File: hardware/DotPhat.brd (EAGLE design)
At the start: 30 x 65 mm, 22 parts, among them CN1 1X4-BIG, J2 RASPBERRYPI-40-PIN-GPIO_PTH, J3 USB-MICROB, U1 ATMEGA328P-MU-QFN32, X3 S4B-ZR

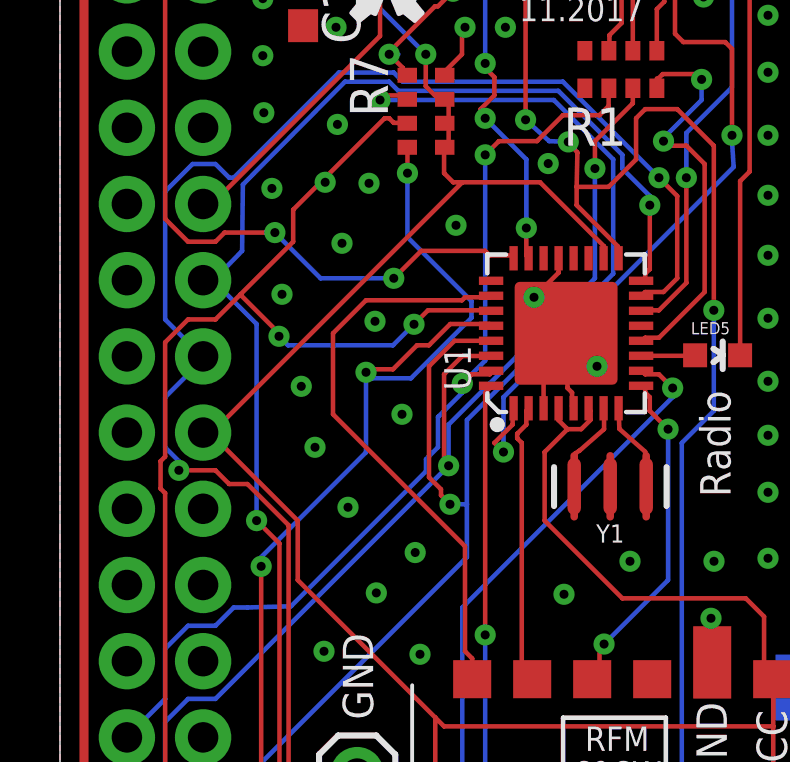
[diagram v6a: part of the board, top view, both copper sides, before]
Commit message: Add TMP112 temperature sensor
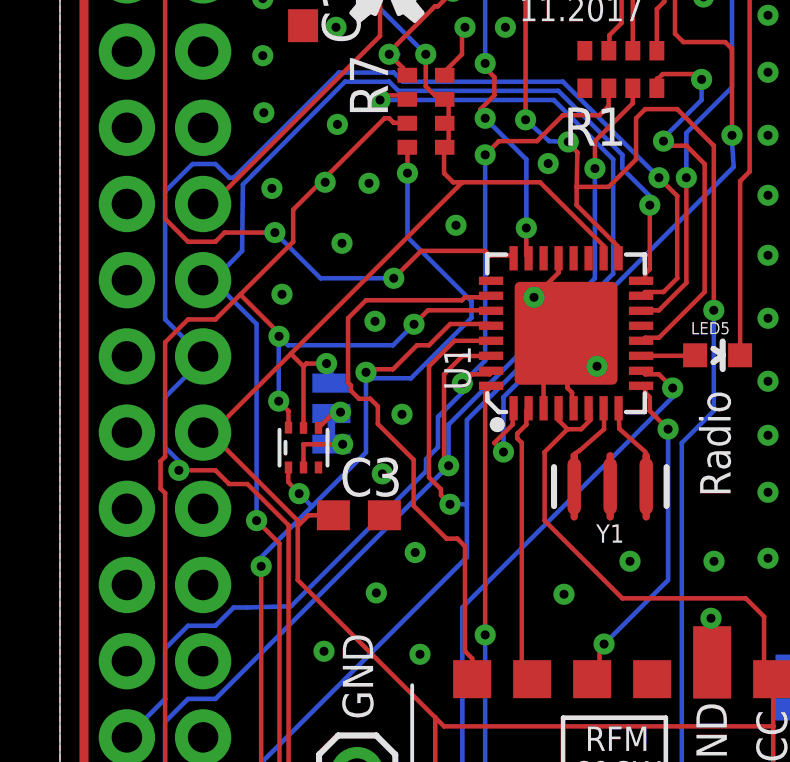
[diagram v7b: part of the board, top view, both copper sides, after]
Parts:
- added C3: 0.1uF, resistor:C0603
- added JP2: JUMPER-SMT_3_1-NC_TRACE_NO-SILK, SparkFun-Jumpers:SMT-JUMPER_3_1-NC_TRACE_NO-SILK
- added U2: TMP102, SparkFun:SOT563
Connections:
- new net N$11: JP2.2, U2.4
- net +3V3: now also C3.1, JP2.1, U2.5
- net GND: now also C3.2, JP2.3, U2.2
- net SCL: now also U2.1
- net SDA: now also U2.6
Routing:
- net +3V3: track 164.0 -> 169.5 mm, vias 3 -> 4
- net SDA: track 48.7 -> 51.9 mm, vias 3 -> 4
- net GND: track 35.2 -> 37.7 mm, vias 119 -> 118
- net SCL: track 41.2 -> 42.8 mm, vias 3 -> 4
- net N$11: track 0.00 -> 1.29 mm, vias 0 -> 1
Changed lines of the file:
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@@
 <setting verticaltext="up"/>
 </settings>
-<grid distance="0.11" unitdist="mil" unit="mil" style="lines" multiple="1" display="yes" altdistance="0.025" altunitdist="inch" altunit="inch"/>
+<grid distance="0.11" unitdist="mil" unit="mm" style="lines" multiple="1" display="yes" altdistance="0.025" altunitdist="inch" altunit="inch"/>
 <layers>
 <layer number="1" name="Top" color="4" fill="1" visible="yes" active="yes"/>
@@
 <element name="C1" library="rcl" package="C0603" value="" x="8.1026" y="43.1038" rot="R270"/>
 <element name="R1" library="SparkFun" package="0603-ARV" value="" x="18.6944" y="40.7924"/>
+<element name="U2" library="SparkFun" package="SOT563" value="TMP102" x="8.11656875" y="28.185871875"/>
+<element name="C3" library="resistor" package="C0603" value="0.1uF" x="9.963403125" y="25.9339125"/>
+<element name="JP2" library="SparkFun-Jumpers" package="SMT-JUMPER_3_1-NC_TRACE_NO-SILK" value="JUMPER-SMT_3_1-NC_TRACE_NO-SILK" x="9.044178125" y="29.32303125" rot="MR270"/>
 </elements>
 <signals>
@@
 <via x="21.8" y="24.4" extent="1-16" drill="0.3"/>
 <via x="21.7" y="22.5" extent="1-16" drill="0.3"/>
-<via x="9.6" y="26.2" extent="1-16" drill="0.3"/>
-<via x="8.5" y="28.2" extent="1-16" drill="0.3"/>
+<via x="10.745540625" y="27.31480625" extent="1-16" drill="0.3"/>
 <via x="19.3" y="15.8" extent="1-16" drill="0.3"/>
 <via x="28.9" y="19.3" extent="1-16" drill="0.3"/>
@@
 <contactref element="X3" pad="1"/>
 <contactref element="U$4" pad="2"/>
-<via x="8.0428" y="30.232" extent="1-16" drill="0.3"/>
 <via x="7.0632" y="36.8288" extent="1-16" drill="0.3"/>
 <via x="9.2476" y="38.9624" extent="1-16" drill="0.3"/>
@@
 <contactref element="C1" pad="2"/>
 <via x="14.8462" y="42.2" extent="1-16" drill="0.3"/>
+<contactref element="U2" pad="2"/>
+<contactref element="C3" pad="2"/>
+<contactref element="JP2" pad="3"/>
+<wire x1="9.044178125" y1="28.30703125" x2="9.42136875" y2="28.30703125" width="0.1524" layer="16"/>
+<wire x1="9.42136875" y1="28.30703125" x2="9.42136875" y2="28.300425" width="0.1524" layer="16"/>
+<via x="9.42136875" y="28.300425" extent="1-16" drill="0.3"/>
+<wire x1="9.42136875" y1="28.300425" x2="8.11656875" y2="28.300425" width="0.1524" layer="1"/>
+<wire x1="8.11656875" y1="28.300425" x2="8.11656875" y2="27.525871875" width="0.1524" layer="1"/>
 </signal>
 <signal name="SDA">
@@
 <wire x1="4.77" y1="10.91" x2="5.9772" y2="9.7028" width="0.1524" layer="16"/>
 <wire x1="5.9772" y1="9.7028" x2="9.906" y2="9.7028" width="0.1524" layer="16"/>
+<contactref element="U2" pad="6"/>
+<wire x1="7.61656875" y1="28.855871875" x2="7.61656875" y2="29.40951875" width="0.1524" layer="1"/>
+<wire x1="7.61656875" y1="29.40951875" x2="7.289546875" y2="29.736540625" width="0.1524" layer="1"/>
+<via x="7.289546875" y="29.736540625" extent="1-16" drill="0.3"/>
+<wire x1="7.289546875" y1="29.736540625" x2="7.289546875" y2="31.889546875" width="0.1524" layer="16"/>
+<wire x1="7.289546875" y1="31.889546875" x2="7.3" y2="31.9" width="0.1524" layer="16"/>
 </signal>
 <signal name="RST">
@@
 <wire x1="14.1256" y1="33.1756" x2="14.37" y2="33.25" width="0.1524" layer="1"/>
 <wire x1="13.716" y1="20.574" x2="13.74" y2="20.47" width="0.1524" layer="1"/>
-<wire x1="13.5" y1="24.9" x2="9.1" y2="29.3" width="0.1524" layer="1"/>
-<wire x1="9.1" y1="29.3" x2="9.1" y2="32" width="0.1524" layer="1"/>
-<wire x1="9.1" y1="32" x2="10.2" y2="33.1" width="0.1524" layer="1"/>
 <wire x1="10.2" y1="33.1" x2="13.4" y2="33.1" width="0.1524" layer="1"/>
 <wire x1="13.4" y1="33.1" x2="13.5" y2="33.2" width="0.1524" layer="1"/>
@@
 <wire x1="13.5" y1="21.4" x2="13.74" y2="21.16" width="0.1524" layer="1"/>
 <wire x1="13.74" y1="21.16" x2="13.74" y2="20.47" width="0.1524" layer="1"/>
+<wire x1="9.966196875" y1="29.81756875" x2="10.3433875" y2="29.81756875" width="0.1524" layer="1"/>
+<wire x1="10.3433875" y1="29.81756875" x2="10.594846875" y2="29.566109375" width="0.1524" layer="1"/>
+<wire x1="10.594846875" y1="29.566109375" x2="10.594846875" y2="28.976578125" width="0.1524" layer="1"/>
+<wire x1="10.594846875" y1="28.976578125" x2="11.7878875" y2="27.7835375" width="0.1524" layer="1"/>
+<wire x1="11.7878875" y1="27.7835375" x2="11.7878875" y2="26.249628125" width="0.1524" layer="1"/>
+<wire x1="11.7878875" y1="26.249628125" x2="12.883134375" y2="25.15438125" width="0.1524" layer="1"/>
+<wire x1="12.883134375" y1="25.15438125" x2="13.24561875" y2="25.15438125" width="0.1524" layer="1"/>
+<wire x1="13.24561875" y1="25.15438125" x2="13.5" y2="24.9" width="0.1524" layer="1"/>
+<wire x1="9.966196875" y1="29.81756875" x2="9.697975" y2="30.085790625" width="0.1524" layer="1"/>
+<wire x1="9.697975" y1="30.085790625" x2="9.697975" y2="30.2618125" width="0.1524" layer="1"/>
+<wire x1="9.697975" y1="30.2618125" x2="9.602978125" y2="30.356809375" width="0.1524" layer="1"/>
+<wire x1="9.602978125" y1="30.356809375" x2="9.602978125" y2="32.502978125" width="0.1524" layer="1"/>
+<wire x1="9.602978125" y1="32.502978125" x2="10.2" y2="33.1" width="0.1524" layer="1"/>
 </signal>
 <signal name="RSCK">
@@
 <wire x1="12.8016" y1="38.1" x2="12.825" y2="38.2" width="0.1524" layer="1"/>
 <wire x1="5.1816" y1="28.8036" x2="4.8768" y2="28.8036" width="0.1524" layer="1"/>
-<wire x1="13.4112" y1="37.0332" x2="5.1816" y2="28.8036" width="0.1524" layer="1"/>
+<wire x1="13.4112" y1="37.0332" x2="7.695309375" y2="31.317309375" width="0.1524" layer="1"/>
+<wire x1="7.695309375" y1="31.317309375" x2="5.1816" y2="28.8036" width="0.1524" layer="1"/>
 <wire x1="12.192" y1="41.3004" x2="10.5156" y2="42.9768" width="0.1524" layer="16"/>
 <wire x1="12.192" y1="40.2336" x2="12.192" y2="41.3004" width="0.1524" layer="1"/>
@@
 <wire x1="7.9248" y1="23.7744" x2="12.5095" y2="19.1897" width="0.1524" layer="1"/>
 <wire x1="12.5095" y1="19.1897" x2="12.8016" y2="18.8976" width="0.1524" layer="1"/>
-<wire x1="7.9248" y1="25.7556" x2="7.9248" y2="23.7744" width="0.1524" layer="1"/>
+<wire x1="7.9248" y1="25.7556" x2="7.9248" y2="25.57348125" width="0.1524" layer="1"/>
+<wire x1="7.9248" y1="25.57348125" x2="7.9248" y2="23.7744" width="0.1524" layer="1"/>
 <wire x1="4.8768" y1="28.8036" x2="7.9248" y2="25.7556" width="0.1524" layer="1"/>
 <wire x1="4.8768" y1="28.8036" x2="4.77" y2="28.69" width="0.1524" layer="1"/>
@@
 <wire x1="8.1026" y1="43.9538" x2="8.2817" y2="43.9538" width="0.1524" layer="1"/>
 <wire x1="8.2817" y1="43.9538" x2="10.1194" y2="45.7915" width="0.1524" layer="1"/>
+<contactref element="C3" pad="1"/>
+<contactref element="U2" pad="5"/>
+<wire x1="8.11656875" y1="28.845871875" x2="8.11656875" y2="30.89605" width="0.1524" layer="1"/>
+<wire x1="8.11656875" y1="30.89605" x2="7.695309375" y2="31.317309375" width="0.1524" layer="1"/>
+<contactref element="JP2" pad="1"/>
+<wire x1="9.113403125" y1="25.9339125" x2="8.28523125" y2="25.9339125" width="0.1524" layer="1"/>
+<wire x1="8.28523125" y1="25.9339125" x2="7.9248" y2="25.57348125" width="0.1524" layer="1"/>
+<wire x1="9.044178125" y1="30.33903125" x2="9.044178125" y2="30.8317875" width="0.1524" layer="16"/>
+<wire x1="9.044178125" y1="30.8317875" x2="8.88491875" y2="30.991046875" width="0.1524" layer="16"/>
+<via x="8.88491875" y="30.991046875" extent="1-16" drill="0.3"/>
+<wire x1="8.88491875" y1="30.991046875" x2="8.211565625" y2="30.991046875" width="0.1524" layer="1"/>
+<wire x1="8.211565625" y1="30.991046875" x2="8.11656875" y2="30.89605" width="0.1524" layer="1"/>
 </signal>
 <signal name="ADCENA">
@@
 <wire x1="11.5824" y1="38.1" x2="11.575" y2="38.2" width="0.1524" layer="1"/>
 <wire x1="14.3256" y1="32.3088" x2="14.37" y2="32.25" width="0.1524" layer="1"/>
-<wire x1="6.7056" y1="24.5364" x2="10.2" y2="28.0308" width="0.1524" layer="16"/>
+<wire x1="6.7056" y1="24.5364" x2="8.396225" y2="26.227025" width="0.1524" layer="16"/>
+<wire x1="8.396225" y1="26.227025" x2="10.2" y2="28.0308" width="0.1524" layer="16"/>
 <wire x1="6.7056" y1="24.2316" x2="6.7056" y2="24.5364" width="0.1524" layer="16"/>
 <wire x1="6.7056" y1="15.0876" x2="6.7056" y2="24.2316" width="0.1524" layer="1"/>
@@
 <wire x1="4.77" y1="13.45" x2="5.9772" y2="12.2428" width="0.1524" layer="16"/>
 <wire x1="5.9772" y1="12.2428" x2="9.906" y2="12.2428" width="0.1524" layer="16"/>
+<contactref element="U2" pad="1"/>
+<wire x1="7.61656875" y1="27.525871875" x2="7.608184375" y2="27.043" width="0.1524" layer="1"/>
+<wire x1="7.608184375" y1="27.043" x2="7.97128125" y2="26.654759375" width="0.1524" layer="1"/>
+<via x="7.97128125" y="26.654759375" extent="1-16" drill="0.3"/>
+<wire x1="7.97128125" y1="26.654759375" x2="7.97128125" y2="26.65196875" width="0.1524" layer="16"/>
+<wire x1="7.97128125" y1="26.65196875" x2="8.396225" y2="26.227025" width="0.1524" layer="16"/>
 </signal>
 <signal name="PUSH">
@@
 <wire x1="21.1528" y1="31.25" x2="21.1702" y2="31.2674" width="0.1524" layer="1"/>
 </signal>
+<signal name="N$11">
+<contactref element="U2" pad="4"/>
+<contactref element="JP2" pad="2"/>
+<via x="9.351515625" y="29.370528125" extent="1-16" drill="0.3"/>
+<wire x1="9.351515625" y1="29.370528125" x2="9.130796875" y2="29.278321875" width="0.1524" layer="16"/>
+<wire x1="9.130796875" y1="29.278321875" x2="9.044178125" y2="29.32303125" width="0.1524" layer="16"/>
+<wire x1="9.351515625" y1="29.370528125" x2="9.141225" y2="29.370528125" width="0.1524" layer="1"/>
+<wire x1="9.141225" y1="29.370528125" x2="8.61656875" y2="28.845871875" width="0.1524" layer="1"/>
+</signal>
 </signals>

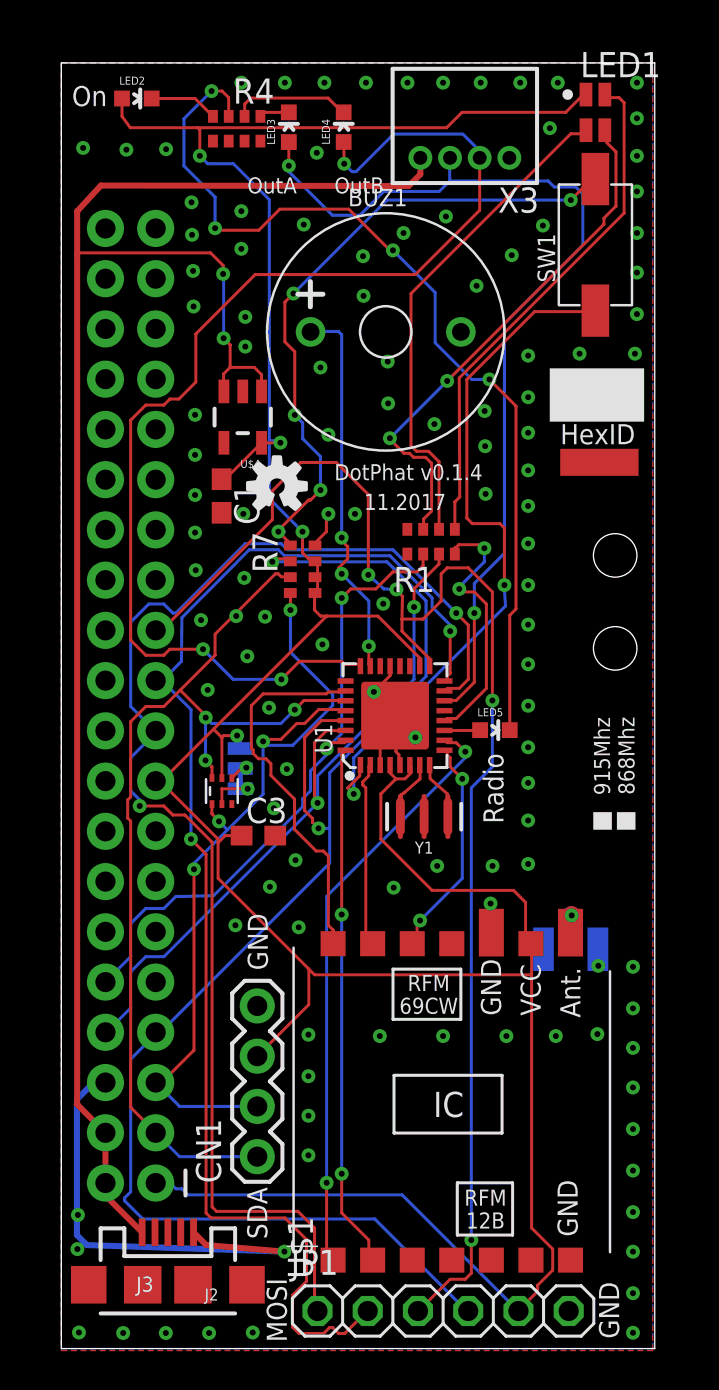
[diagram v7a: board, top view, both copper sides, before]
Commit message: Add USB programming connections
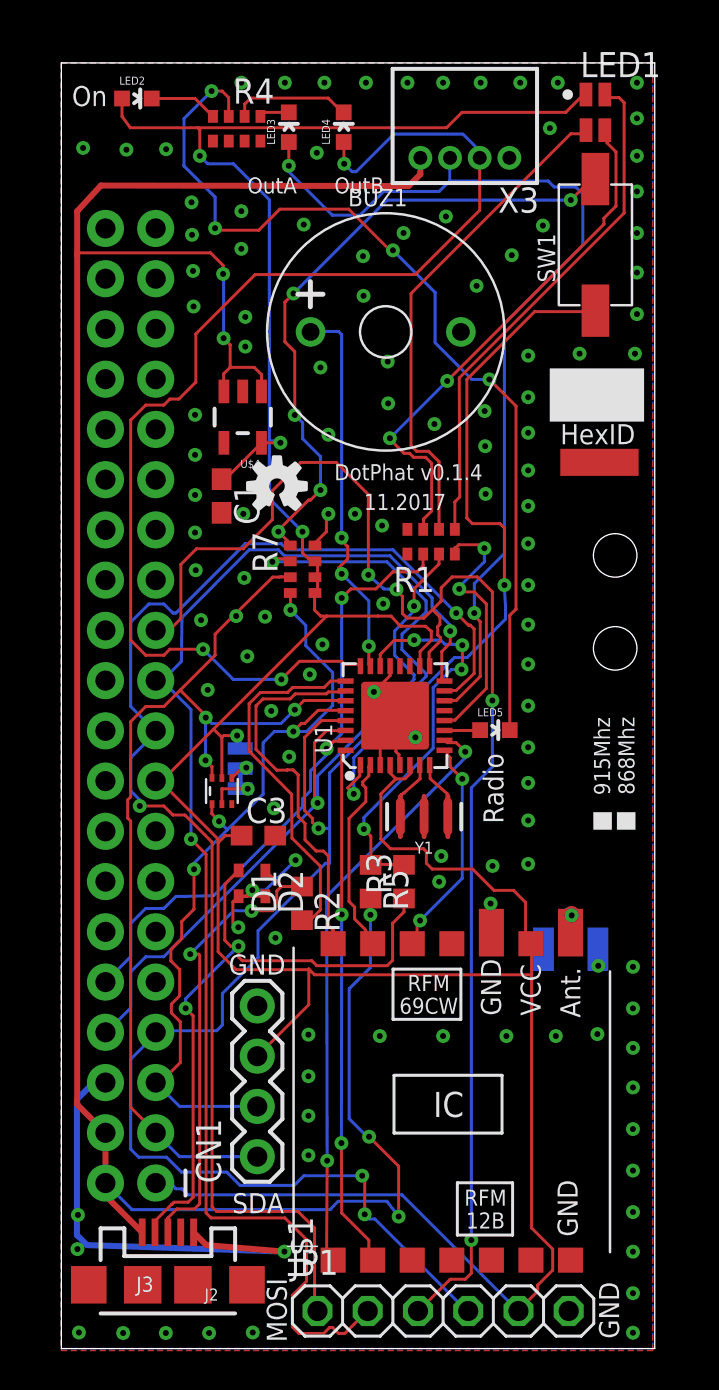
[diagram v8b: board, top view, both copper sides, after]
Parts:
- added D1, D2: (no value), diode:SOD523
- added R2, R3, R5: (no value), rcl:R0603
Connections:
- new net USB_D+: D2.C, J3.D+, R2.1
- new net USB_D-: D1.C, J3.D-, R3.1
- net +5V: now also R5.2
- net GND: now also D1.A, D2.A
- net LIGHT_SENSE: now also R3.2, R5.1
- net MOVE_INT: now also R2.2
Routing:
- net +5V: track 88.9 -> 123.1 mm, vias 2 -> 5
- net USB_D-: track 0.00 -> 33.6 mm, vias 0 -> 2
- net USB_D+: track 0.00 -> 24.4 mm, vias 0 -> 2
- net LIGHT_SENSE: track 0.00 -> 20.4 mm, vias 0 -> 4
- net MOVE_INT: track 0.00 -> 18.4 mm
- net GND: track 37.7 -> 44.6 mm, vias 118 -> 120
- net +3V3: track 169.5 -> 173.6 mm
- net RST: track 74.1 -> 76.3 mm, vias 2 -> 4
- net SCK: track 71.4 -> 72.9 mm
- net SCL: track 42.8 -> 42.0 mm
- net RXD: track 36.7 -> 37.5 mm
- net RSCK: track 9.38 -> 10.1 mm
